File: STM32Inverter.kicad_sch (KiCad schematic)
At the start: 102 parts, among them J1 STLINK, J2 CURRENT SENSE, J5 UART, J6 INTERFACE, J7 POWER, J8 501571-2007, J9 RESOLVER, Q4 ST3422A, U1 STM32F303VCTx, U10 ULN2002, U11 LM393, U12 LM393, U4 74HCT00, U7 MCP2551-I-SN, Y3 CSTNE8M00GH5C000R0

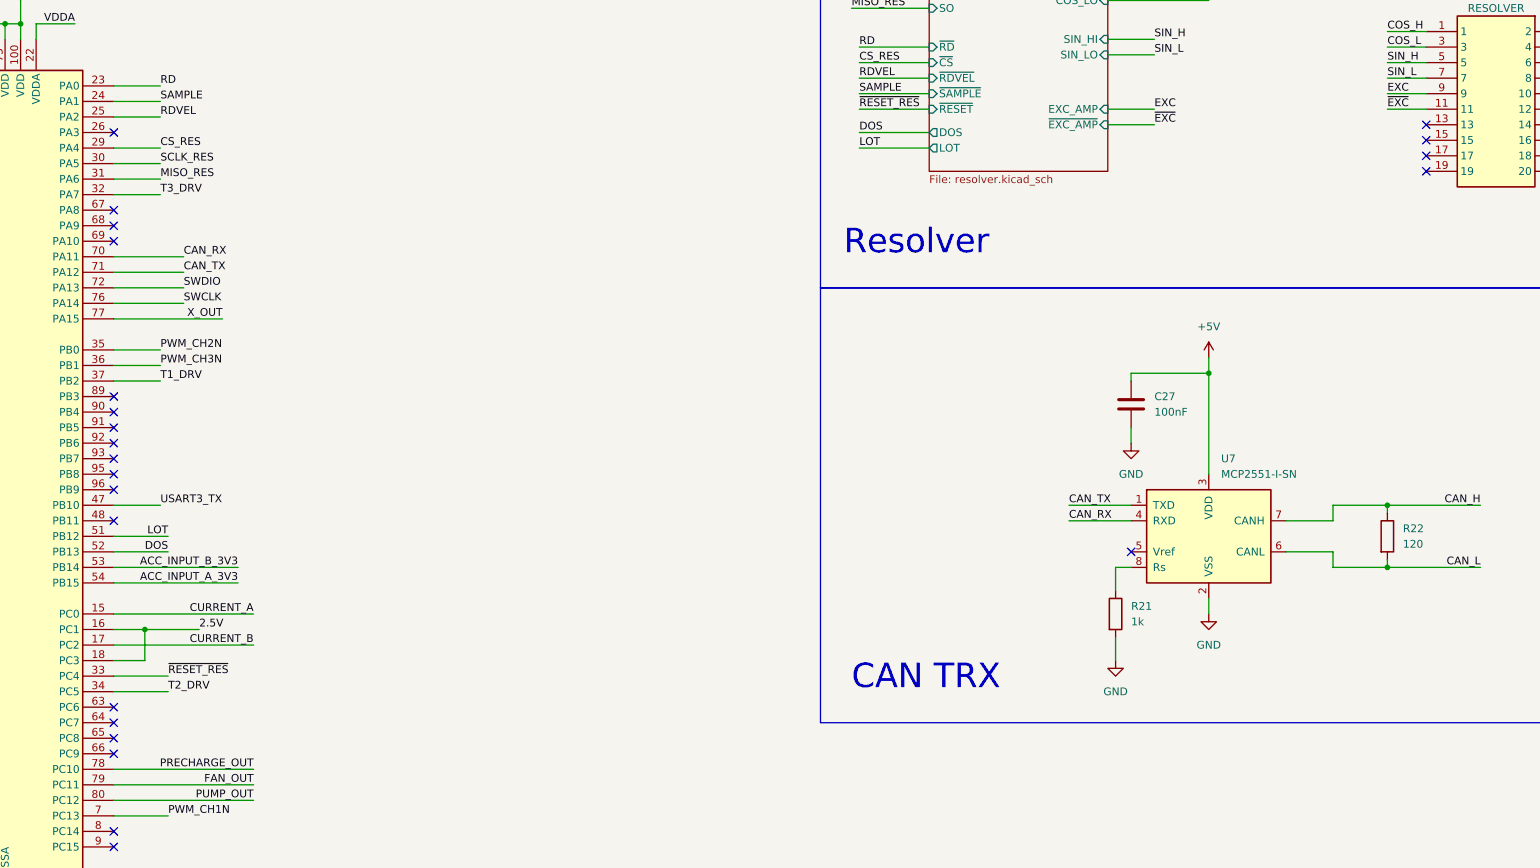
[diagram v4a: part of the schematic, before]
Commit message: added GPIO. Deploy
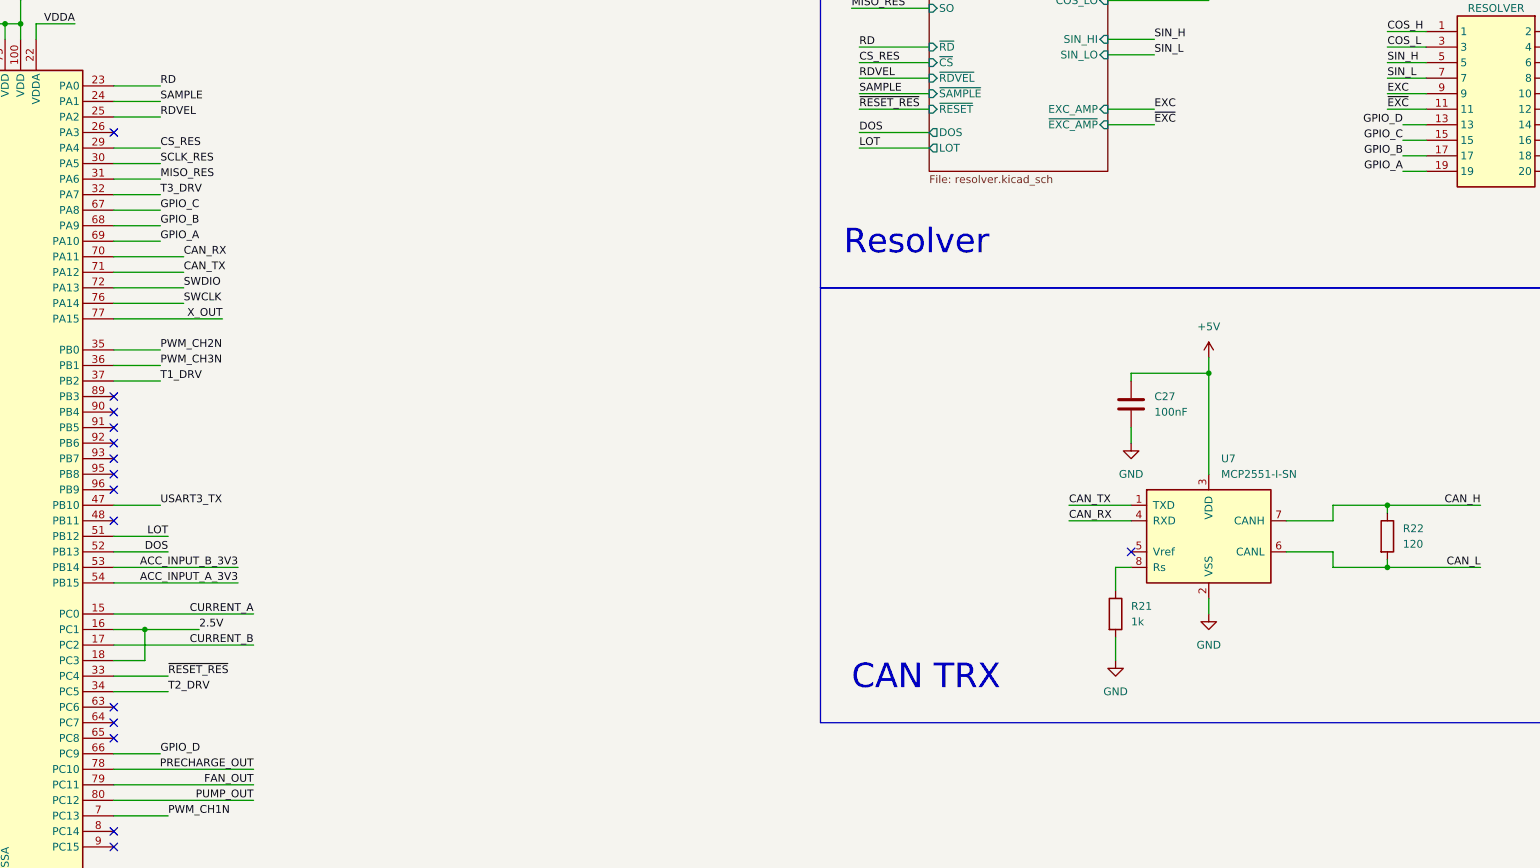
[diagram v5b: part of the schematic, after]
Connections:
- net GPIO_D: now reaches U1.66 (PC9)
- net GPIO_D: now also J9.13
- net GPIO_C: now reaches U1.67 (PA8)
- net GPIO_C: now also J9.15
- net GPIO_B: now reaches U1.68 (PA9)
- net GPIO_B: now also J9.17
- net GPIO_A: now reaches U1.69 (PA10)
- net GPIO_A: now also J9.19
- no-connect marks 53 -> 45
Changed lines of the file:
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@@
   (no_connect (at 233.68 181.61))
   (no_connect (at 233.68 227.33))
-  (no_connect (at 488.95 149.86))
   (no_connect (at 233.68 184.15))
   (no_connect (at 233.68 179.07))
   (no_connect (at 233.68 204.47))
-  (no_connect (at 488.95 152.4))
   (no_connect (at 236.22 60.96))
   (no_connect (at 511.81 152.4))
@@
   (no_connect (at 274.32 245.11))
   (no_connect (at 414.02 93.98))
-  (no_connect (at 488.95 144.78))
   (no_connect (at 274.32 194.31))
-  (no_connect (at 274.32 163.83))
-  (no_connect (at 488.95 147.32))
   (no_connect (at 233.68 166.37))
-  (no_connect (at 274.32 161.29))
   (no_connect (at 274.32 260.35))
   (no_connect (at 233.68 229.87))
   (no_connect (at 233.68 252.73))
   (no_connect (at 233.68 176.53))
-  (no_connect (at 274.32 158.75))
   (no_connect (at 233.68 224.79))
   (no_connect (at 274.32 242.57))
@@
   (no_connect (at 233.68 255.27))
   (no_connect (at 233.68 232.41))
-  (no_connect (at 274.32 247.65))
   (no_connect (at 256.54 60.96))
   (wire (pts (xy 116.84 39.37) (xy 120.65 39.37))
@@
     (stroke (width 0) (type default))
   )
+  (wire (pts (xy 485.14 147.32) (xy 488.95 147.32))
+    (stroke (width 0) (type default))
+  )
   (wire (pts (xy 35.56 170.18) (xy 35.56 172.72))
     (stroke (width 0) (type default))
@@
     (stroke (width 0) (type default))
   )
+  (wire (pts (xy 281.94 158.75) (xy 274.32 158.75))
+    (stroke (width 0) (type default))
+  )
   (wire (pts (xy 196.85 72.39) (xy 196.85 69.85))
     (stroke (width 0) (type default))
@@
     (stroke (width 0) (type default))
   )
+  (wire (pts (xy 485.14 149.86) (xy 488.95 149.86))
+    (stroke (width 0) (type default))
+  )
   (wire (pts (xy 143.51 316.23) (xy 143.51 313.69))
     (stroke (width 0) (type default))
@@
     (stroke (width 0) (type default))
   )
+  (wire (pts (xy 281.94 161.29) (xy 274.32 161.29))
+    (stroke (width 0) (type default))
+  )
   (wire (pts (xy 237.49 339.09) (xy 237.49 337.82))
     (stroke (width 0) (type default))
@@
     (stroke (width 0) (type default))
   )
+  (wire (pts (xy 485.14 144.78) (xy 488.95 144.78))
+    (stroke (width 0) (type default))
+  )
   (wire (pts (xy 201.93 364.49) (xy 204.47 364.49))
     (stroke (width 0) (type default))
@@
     (stroke (width 0) (type default))
   )
+  (wire (pts (xy 281.94 163.83) (xy 274.32 163.83))
+    (stroke (width 0) (type default))
+  )
   (wire (pts (xy 35.56 219.71) (xy 43.18 219.71))
     (stroke (width 0) (type default))
@@
     (stroke (width 0) (type default))
   )
+  (wire (pts (xy 485.14 152.4) (xy 488.95 152.4))
+    (stroke (width 0) (type default))
+  )
   (wire (pts (xy 224.79 163.83) (xy 233.68 163.83))
+    (stroke (width 0) (type default))
+  )
+  (wire (pts (xy 281.94 247.65) (xy 274.32 247.65))
     (stroke (width 0) (type default))
   )
@@
     (effects (font (size 4 4)) (justify left bottom))
   )
+  (label "GPIO_C" (at 485.14 147.32 180) (fields_autoplaced)
+    (effects (font (size 1.27 1.27)) (justify right bottom))
+  )
   (label "SCLK_RES" (at 281.94 151.13 0) (fields_autoplaced)
     (effects (font (size 1.27 1.27)) (justify left bottom))
@@
     (effects (font (size 1.27 1.27)) (justify left bottom))
   )
+  (label "GPIO_D" (at 281.94 247.65 0) (fields_autoplaced)
+    (effects (font (size 1.27 1.27)) (justify left bottom))
+  )
   (label "PRECHARGE_OUT" (at 219.71 50.8 0) (fields_autoplaced)
     (effects (font (size 1.27 1.27)) (justify left bottom))
@@
     (effects (font (size 1.27 1.27)) (justify right bottom))
   )
+  (label "GPIO_A" (at 485.14 152.4 180) (fields_autoplaced)
+    (effects (font (size 1.27 1.27)) (justify right bottom))
+  )
   (label "CAN_L" (at 497.84 217.17 180) (fields_autoplaced)
     (effects (font (size 1.27 1.27)) (justify right bottom))
@@
     (effects (font (size 1.27 1.27)) (justify left bottom))
   )
+  (label "GPIO_B" (at 281.94 161.29 0) (fields_autoplaced)
+    (effects (font (size 1.27 1.27)) (justify left bottom))
+  )
   (label "POS_CURRENT_SETPOINT" (at 69.85 177.8 0) (fields_autoplaced)
     (effects (font (size 1.27 1.27)) (justify left bottom))
@@
     (effects (font (size 1.27 1.27)) (justify left bottom))
   )
+  (label "GPIO_A" (at 281.94 163.83 0) (fields_autoplaced)
+    (effects (font (size 1.27 1.27)) (justify left bottom))
+  )
   (label "VBUS_DRV" (at 577.85 62.23 180) (fields_autoplaced)
     (effects (font (size 1.27 1.27)) (justify right bottom))
@@
     (effects (font (size 1.27 1.27)) (justify left bottom))
   )
+  (label "GPIO_B" (at 485.14 149.86 180) (fields_autoplaced)
+    (effects (font (size 1.27 1.27)) (justify right bottom))
+  )
   (label "FAULT_DRV" (at 127 171.45 0) (fields_autoplaced)
     (effects (font (size 1.27 1.27)) (justify left bottom))
@@
     (effects (font (size 1.27 1.27)) (justify left bottom))
   )
+  (label "GPIO_C" (at 281.94 158.75 0) (fields_autoplaced)
+    (effects (font (size 1.27 1.27)) (justify left bottom))
+  )
   (label "LOT" (at 396.24 148.59 0) (fields_autoplaced)
     (effects (font (size 1.27 1.27)) (justify left bottom))
@@
     (effects (font (size 1.27 1.27)) (justify left bottom))
   )
+  (label "GPIO_D" (at 485.14 144.78 180) (fields_autoplaced)
+    (effects (font (size 1.27 1.27)) (justify right bottom))
+  )
   (label "SIN_H" (at 482.6 134.62 0) (fields_autoplaced)

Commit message: BOM
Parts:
- C17, C29, C30, C8: LCSC (none) -> C913534
- C21: LCSC (none) -> C2162694
- C27: value 100nF -> 100n; LCSC (none) -> C913534
- C6: LCSC (none) -> C597236
- D5: Field4 (none) -> mamy
- D9: LCSC (none) -> PESD3V3L5UY
- F1, F2, F3, F4: LCSC (none) -> C207021
- F5: LCSC (none) -> C310935
- H1, H2, H3, H4, J1, J5: LCSC (none) -> none
- J2, J6, J7, J8, J9: LCSC (none) -> mouser
- Q4: LCSC (none) -> C2682907
- TH1: LCSC SDNT2012X473J3950HTF -> C2991770
- U10: Field4 C5252903 -> (none); LCSC (none) -> C5252903
- U7: LCSC (none) -> C623210
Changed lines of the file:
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@@
       (effects (font (size 1.27 1.27)) hide)
     )
+    (property "LCSC" "PESD3V3L5UY" (at 110.49 72.39 0)
+      (effects (font (size 1.27 1.27)) hide)
+    )
     (pin "1")
     (pin "2")
@@
       (effects (font (size 1.27 1.27)) hide)
     )
+    (property "LCSC" "PESD3V3L5UY" (at 142.24 72.39 0)
+      (effects (font (size 1.27 1.27)) hide)
+    )
     (pin "1")
     (pin "2")
@@
       (effects (font (size 1.27 1.27)) hide)
     )
+    (property "LCSC" "PESD3V3L5UY" (at 168.91 74.93 0)
+      (effects (font (size 1.27 1.27)) hide)
+    )
     (pin "1")
     (pin "2")
@@
       (effects (font (size 1.27 1.27)) (justify left top) hide)
     )
+    (property "LCSC" "mouser" (at 97.79 26.67 0)
+      (effects (font (size 1.27 1.27)) hide)
+    )
     (pin "1")
     (pin "10")
@@
       (effects (font (size 1.27 1.27)) hide)
     )
+    (property "LCSC" "none" (at 295.91 330.2 0)
+      (effects (font (size 1.27 1.27)) hide)
+    )
     (pin "1")
     (pin "2")
@@
       (effects (font (size 1.27 1.27)) hide)
     )
+    (property "LCSC" "none" (at 209.55 367.03 0)
+      (effects (font (size 1.27 1.27)) hide)
+    )
     (pin "1")
     (pin "2")
@@
       (effects (font (size 1.27 1.27)) hide)
     )
+    (property "LCSC" "C913534" (at 215.9 143.51 0)
+      (effects (font (size 1.27 1.27)) hide)
+    )
     (pin "1")
     (pin "2")
@@
       (effects (font (size 1.27 1.27)) hide)
     )
+    (property "LCSC" "C207021 " (at 132.08 44.45 0)
+      (effects (font (size 1.27 1.27)) hide)
+    )
     (pin "1")
     (pin "2")
@@
       (effects (font (size 1.27 1.27)) hide)
     )
+    (property "LCSC" "C913534" (at 31.75 73.66 0)
+      (effects (font (size 1.27 1.27)) hide)
+    )
     (pin "1")
     (pin "2")
@@
       (effects (font (size 1.27 1.27)) (justify left top) hide)
     )
+    (property "LCSC" "mouser" (at 504.19 58.42 0)
+      (effects (font (size 1.27 1.27)) hide)
+    )
     (pin "1")
     (pin "10")
@@
       (effects (font (size 1.27 1.27)) hide)
     )
+    (property "LCSC" "C207021 " (at 128.27 300.99 0)
+      (effects (font (size 1.27 1.27)) hide)
+    )
     (pin "1")
     (pin "2")
@@
       (effects (font (size 1.27 1.27)) hide)
     )
+    (property "LCSC" "C207021 " (at 77.47 313.69 0)
+      (effects (font (size 1.27 1.27)) hide)
+    )
     (pin "1")
     (pin "2")
@@
       (effects (font (size 1.27 1.27)) (justify left top) hide)
     )
+    (property "LCSC" "mouser" (at 36.83 120.65 0)
+      (effects (font (size 1.27 1.27)) hide)
+    )
     (pin "1")
     (pin "2")
@@
       (effects (font (size 1.27 1.27)) hide)
     )
+    (property "LCSC" "PESD3V3L5UY" (at 44.45 72.39 0)
+      (effects (font (size 1.27 1.27)) hide)
+    )
     (pin "1")
     (pin "2")
@@
       (effects (font (size 1.27 1.27)) hide)
     )
+    (property "LCSC" "none" (at 256.54 367.03 0)
+      (effects (font (size 1.27 1.27)) hide)
+    )
     (pin "1")
     (instances
@@
       (effects (font (size 1.27 1.27)) hide)
     )
+    (property "LCSC" "C913534" (at 97.79 73.66 0)
+      (effects (font (size 1.27 1.27)) hide)
+    )
     (pin "1")
     (pin "2")
@@
       (effects (font (size 1.27 1.27)) hide)
     )
+    (property "LCSC" "PESD3V3L5UY" (at 196.85 74.93 0)
+      (effects (font (size 1.27 1.27)) hide)
+    )
     (pin "1")
     (pin "2")
@@
       (effects (font (size 1.27 1.27)) (justify left))
     )
-    (property "Value" "100nF" (at 444.5 191.7699 0)
+    (property "Value" "100n" (at 444.5 191.7699 0)
       (effects (font (size 1.27 1.27)) (justify left))
     )
@@
       (effects (font (size 1.27 1.27)) hide)
     )
+    (property "LCSC" "C913534" (at 440.69 190.5 0)
+      (effects (font (size 1.27 1.27)) hide)
+    )
     (pin "1")
     (pin "2")
@@
       (effects (font (size 1.27 1.27)) hide)
     )
+    (property "LCSC" "C207021 " (at 104.14 308.61 0)
+      (effects (font (size 1.27 1.27)) hide)
+    )
     (pin "1")
     (pin "2")
@@
       (effects (font (size 1.27 1.27)) hide)
     )
+    (property "LCSC" "none" (at 250.19 367.03 0)
+      (effects (font (size 1.27 1.27)) hide)
+    )
     (pin "1")
     (instances
@@
       (effects (font (size 1.27 1.27)) hide)
     )
+    (property "LCSC" "C597236" (at 80.01 350.52 0)
+      (effects (font (size 1.27 1.27)) hide)
+    )
     (pin "1")
     (pin "2")
@@
       (effects (font (size 1.27 1.27)) hide)
     )
+    (property "LCSC" "none" (at 242.57 367.03 0)
+      (effects (font (size 1.27 1.27)) hide)
+    )
     (pin "1")
     (instances
@@
       (effects (font (size 1.27 1.27)) hide)
     )
+    (property "LCSC" "C310935" (at 92.71 266.7 0)
+      (effects (font (size 1.27 1.27)) hide)
+    )
     (pin "1")
     (pin "2")
@@
       (effects (font (size 1.27 1.27)) hide)
     )
+    (property "LCSC" "C2162694" (at 90.17 320.04 0)
+      (effects (font (size 1.27 1.27)) hide)
+    )
     (pin "1")
     (pin "2")
@@
       (effects (font (size 1.27 1.27)) hide)
     )
+    (property "LCSC" "none" (at 236.22 367.03 0)
+      (effects (font (size 1.27 1.27)) hide)
+    )
     (pin "1")
     (instances
@@
       (effects (font (size 1.27 1.27)) (justify left top) hide)
     )
+    (property "LCSC" "mouser" (at 511.81 129.54 0)
+      (effects (font (size 1.27 1.27)) hide)
+    )
     (pin "1")
     (pin "10")
@@
       (effects (font (size 1.27 1.27)) hide)
     )
+    (property "Field4" "mamy" (at 204.47 336.55 0)
+      (effects (font (size 1.27 1.27)) hide)
+    )
     (pin "1")
     (pin "2")
@@
       (effects (font (size 1.27 1.27)) hide)
     )
+    (property "LCSC" "C2682907" (at 284.48 81.28 0)
+      (effects (font (size 1.27 1.27)) hide)
+    )
     (pin "1")
     (pin "2")
@@
       (effects (font (size 1.27 1.27)) hide)
     )
+    (property "LCSC" "C623210" (at 453.39 212.09 0)
+      (effects (font (size 1.27 1.27)) hide)
+    )
     (pin "1")
     (pin "2")
@@
       (effects (font (size 1.27 1.27)) hide)
     )
-    (property "Field4" "C5252903" (at 246.38 50.8 0)
+    (property "Field4" "" (at 246.38 50.8 0)
+      (effects (font (size 1.27 1.27)) hide)
+    )
+    (property "LCSC" "C5252903" (at 246.38 50.8 0)
       (effects (font (size 1.27 1.27)) hide)
     )
@@
       (effects (font (size 1.27 1.27)) hide)
     )
-    (property "LCSC" "SDNT2012X473J3950HTF" (at 279.4 377.19 0)
+    (property "LCSC" "C2991770" (at 279.4 377.19 0)
       (effects (font (size 1.27 1.27)) hide)
     )
@@
       (effects (font (size 1.27 1.27)) (justify left top) hide)
     )
+    (property "LCSC" "mouser" (at 46.99 300.99 0)
+      (effects (font (size 1.27 1.27)) hide)
+    )
     (pin "1")
     (pin "2")
@@
       (effects (font (size 1.27 1.27)) hide)
     )
+    (property "LCSC" "C913534" (at 128.27 74.93 0)
+      (effects (font (size 1.27 1.27)) hide)
+    )

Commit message: Zabawy z Krzysztofem. Silnik kręcony
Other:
- note added: "zamienić postive i negative currerent setpoint"
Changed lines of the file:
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@@
     (effects (font (size 4 4)) (justify left bottom))
+  )
+  (text "zamienić postive i negative currerent setpoint" (at 48.26 203.2 0)
+    (effects (font (size 1.27 1.27)) (justify left bottom))
   )
   (text "Current Sensing" (at 25.4 250.19 0)
